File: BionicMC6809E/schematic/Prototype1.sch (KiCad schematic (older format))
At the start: 5 parts, among them J1 BionicConnector, U1 MC6809EP, U2 74HCT126

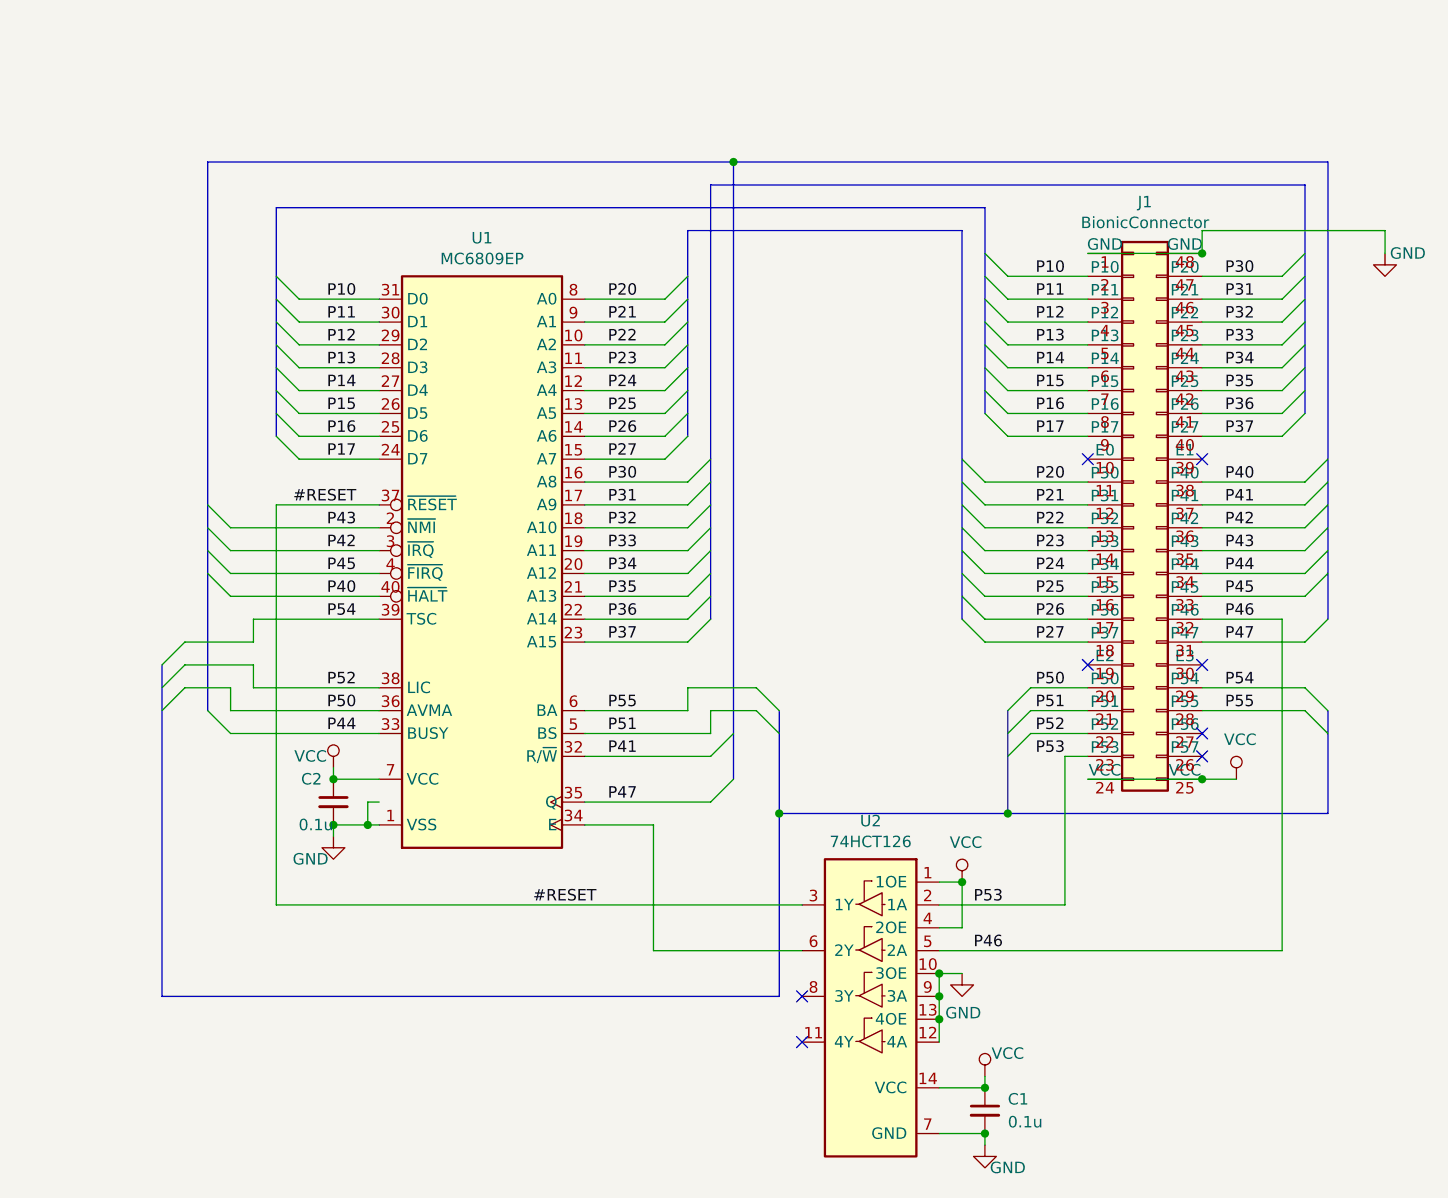
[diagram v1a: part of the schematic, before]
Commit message: [BionicMC6809E] Tune bus cycle
- Teensy 4.1: Q/E ~ 1.0MHz
- Teensy 3.5: Q/E ~ 230kHz
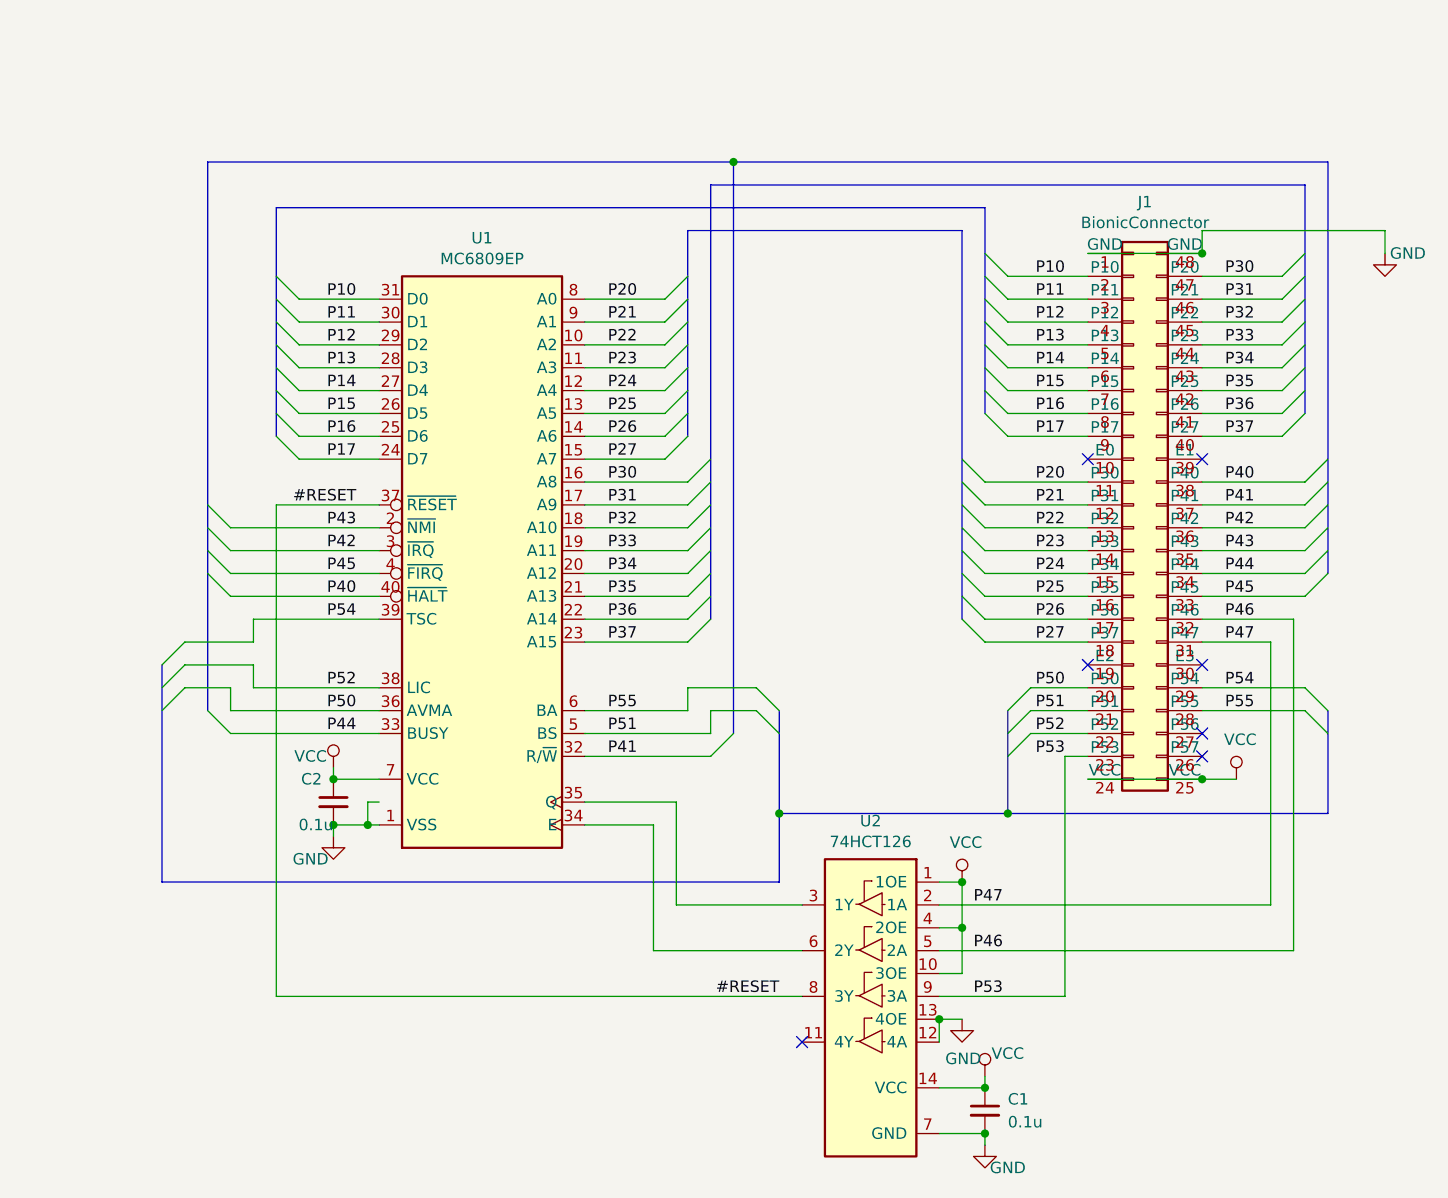
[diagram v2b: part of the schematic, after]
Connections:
- net #RESET: now also U2.8 (3Y); no longer U2.3 (1Y)
- net GND: no longer U2.10 (3OE), U2.9 (3A)
- net P47: now also U2.2 (1A); no longer U1.35 (Q)
- net P53: now also U2.9 (3A); no longer U2.2 (1A)
- net VCC: now also U2.10 (3OE)
- new net: U1.35 (Q), U2.3 (1Y)
- no-connect marks 8 -> 7
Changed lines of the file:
@@
 Sheet 1 1
 Title "BionicMC6809E Mezzanine"
-Date "2021-11-12"
-Rev "1"
+Date "2021-11-25"
+Rev "2"
 Comp "Tadashi G. Takaoka"
 Comment1 ""
@@
 Wire Wire Line
 	7750 2600 7400 2600
-Text Label 6400 4650 0    50   ~ 0
+Text Label 6400 5050 0    50   ~ 0
 P53
 Text Label 3700 3000 2    50   ~ 0
@@
 	1    0    0    -1
 $EndComp
-NoConn ~ 5650 5050
 NoConn ~ 5650 5250
-Text Label 4750 4650 2    50   ~ 0
+Text Label 5550 5050 2    50   ~ 0
 #RESET
 Text Label 3700 2900 2    50   ~ 0
@@
 Entry Wire Line
 	3050 3000 3150 3100
-Entry Wire Line
-	5350 4100 5250 4200
 Text Label 7500 2800 0    50   ~ 0
 P40
@@
 	7400 3300 7850 3300
 Wire Wire Line
-	7400 3500 7850 3500
+	7400 3500 7700 3500
 Entry Wire Line
 	7950 2700 7850 2800
@@
 Entry Wire Line
 	7950 3200 7850 3300
-Entry Wire Line
-	7950 3400 7850 3500
 $Comp
 L power:GND #PWR06
 U 1 1 61A0F5E3
-P 6350 4950
-F 0 "#PWR06" H 6350 4700 50  0001 C CNN
-F 1 "GND" H 6355 4777 50  0000 C CNN
-F 2 "" H 6350 4950 50  0001 C CNN
-F 3 "" H 6350 4950 50  0001 C CNN
-	1    6350 4950
+P 6350 5150
+F 0 "#PWR06" H 6350 4900 50  0001 C CNN
+F 1 "GND" H 6355 4977 50  0000 C CNN
+F 2 "" H 6350 5150 50  0001 C CNN
+F 3 "" H 6350 5150 50  0001 C CNN
+	1    6350 5150
 	1    0    0    -1
 $EndComp
@@
 Text Label 4800 3800 0    50   ~ 0
 P55
-Text Label 4800 4200 0    50   ~ 0
+Text Label 6400 4650 0    50   ~ 0
 P47
-Wire Wire Line
-	5250 4200 4700 4200
 Text Label 3700 3700 2    50   ~ 0
 P52
@@
 Wire Wire Line
 	6250 5250 6250 5150
-Connection ~ 6250 5050
-Wire Wire Line
-	6250 5050 6250 4950
-Connection ~ 6250 5150
-Wire Wire Line
-	6250 5150 6250 5050
-Wire Wire Line
-	6800 4000 6800 4650
 Wire Wire Line
 	3800 3300 3150 3300
@@
 $EndComp
 Wire Wire Line
-	6250 4950 6350 4950
-Connection ~ 6250 4950
-Wire Wire Line
 	6350 4750 6250 4750
 Connection ~ 6350 4550
@@
 	6350 4550 6350 4750
 Wire Wire Line
-	7400 3400 7750 3400
-Wire Wire Line
-	7750 3400 7750 4850
-Wire Wire Line
-	7750 4850 6250 4850
-Text Label 6400 4850 0    50   ~ 0
-P46
+	7400 3400 7800 3400
+Wire Wire Line
+	7800 3400 7800 4850
+Wire Wire Line
+	7800 4850 6250 4850
 Wire Wire Line
 	4700 4300 5000 4300
@@
 Wire Bus Line
 	3350 1600 6450 1600
-Wire Bus Line
-	3050 1400 5350 1400
-Connection ~ 5350 1400
-Wire Bus Line
-	5350 1400 7950 1400
 Entry Wire Line
 	3150 3900 3050 3800
@@
 	3800 3900 3150 3900
 Wire Wire Line
-	3350 2900 3350 4650
-Wire Wire Line
 	3350 2900 3800 2900
 Wire Wire Line
-	3350 4650 5650 4650
+	3350 5050 5650 5050
 Text Label 3700 3800 2    50   ~ 0
 P50
@@
 Wire Wire Line
 	6800 4000 6900 4000
-Wire Wire Line
-	6250 4650 6800 4650
 Entry Wire Line
 	6550 3800 6650 3700
@@
 	6550 4250 5550 4250
 Wire Bus Line
-	5550 4250 5550 5050
-Wire Bus Line
-	5550 5050 2850 5050
-Wire Bus Line
-	5350 1400 5350 4100
+	5550 4250 5550 4550
+Wire Bus Line
+	5550 4550 2850 4550
+Connection ~ 5550 4250
+Wire Wire Line
+	6250 5150 6350 5150
+Connection ~ 6250 5150
+Text Label 6400 4850 0    50   ~ 0
+P46
+Wire Wire Line
+	6350 4750 6350 4950
+Wire Wire Line
+	6350 4950 6250 4950
+Connection ~ 6350 4750
+Wire Wire Line
+	6800 5050 6250 5050
+Wire Wire Line
+	6800 4000 6800 5050
+Wire Wire Line
+	7700 3500 7700 4650
+Wire Wire Line
+	7700 4650 6250 4650
+Wire Wire Line
+	3350 2900 3350 5050
+Wire Bus Line
+	3050 1400 5350 1400
+Wire Wire Line
+	5100 4200 5100 4650
+Wire Wire Line
+	5100 4650 5650 4650
+Wire Wire Line
+	5100 4200 4700 4200
+Wire Bus Line
+	5350 3900 5350 1400
 Wire Bus Line
 	7950 3800 7950 4250
@@
 	5550 3800 5550 4250
 Wire Bus Line
-	2850 3600 2850 5050
+	2850 3600 2850 4550
 Wire Bus Line
 	6550 3800 6550 4250
@@
 	3050 1400 3050 3800
 Wire Bus Line
-	7950 1400 7950 3400
+	7950 1400 7950 3200
 Wire Bus Line
 	5250 1500 5250 3400
@@
 Wire Bus Line
 	3350 1600 3350 2600
-Connection ~ 5550 4250
+Connection ~ 5350 1400
+Wire Bus Line
+	5350 1400 7950 1400
 $EndSCHEMATC

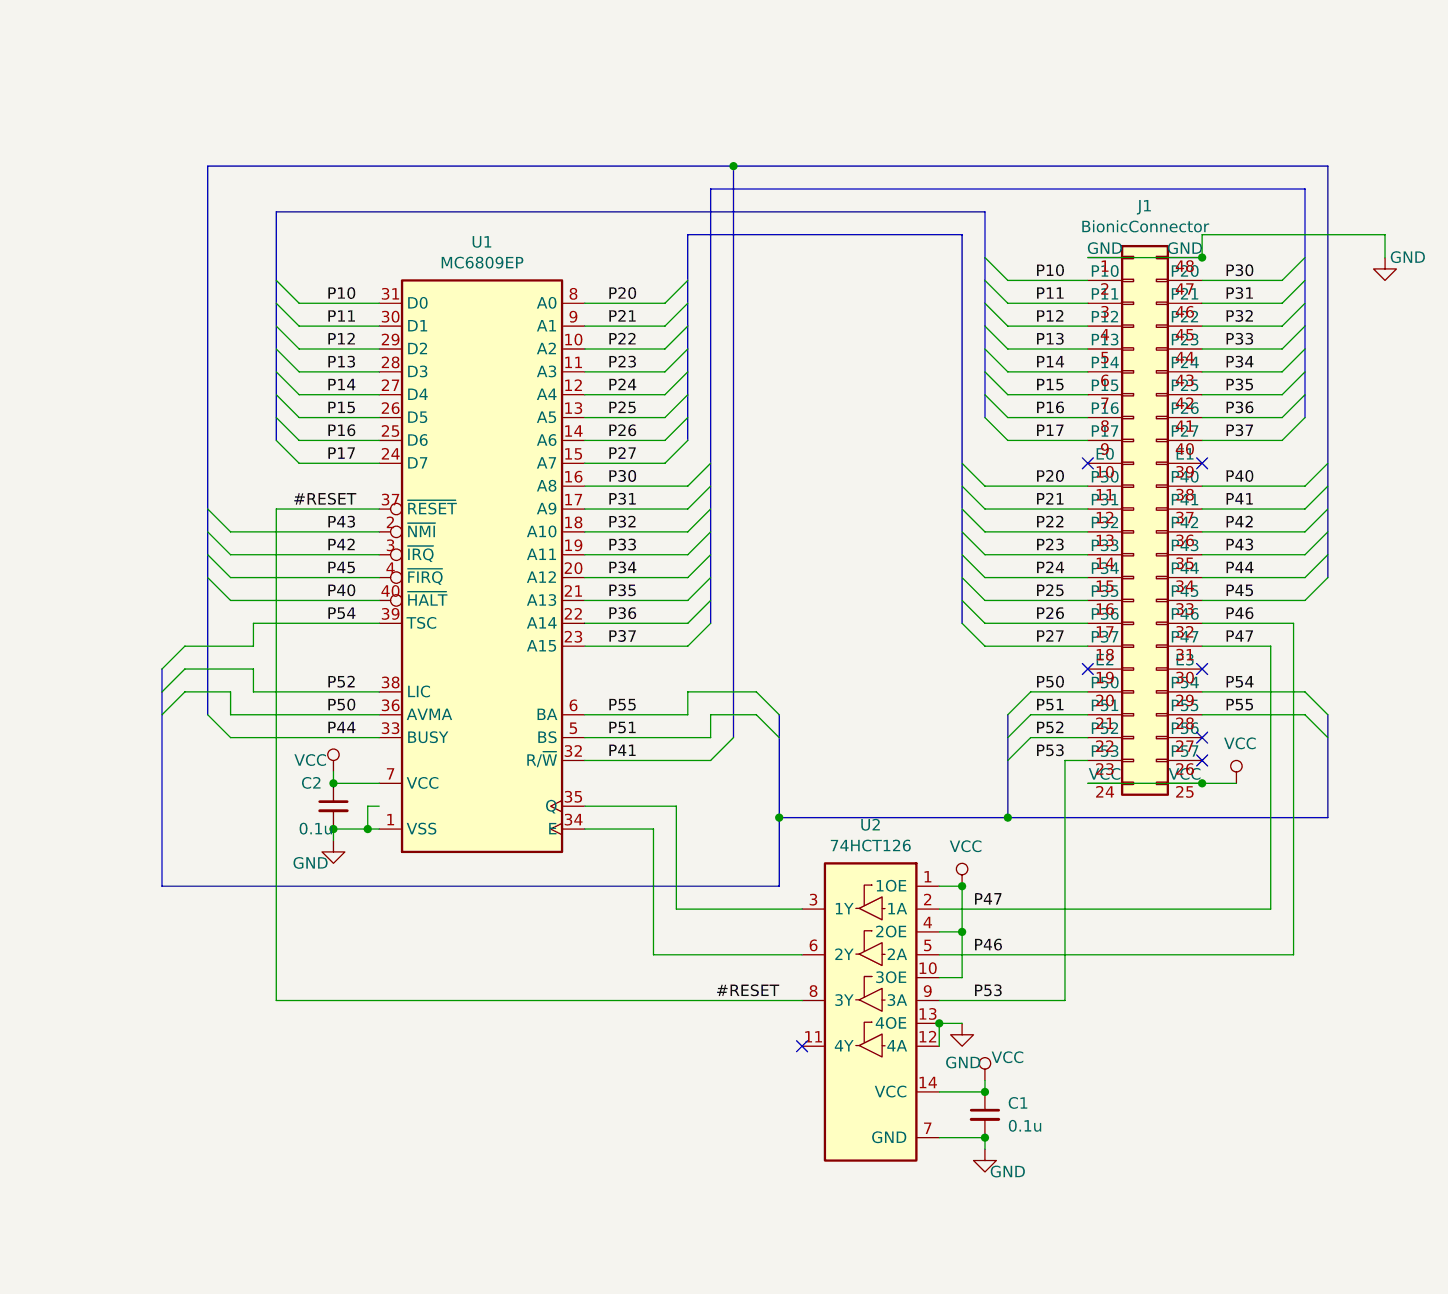
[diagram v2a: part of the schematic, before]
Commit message: Fix Bionic connector pin outs
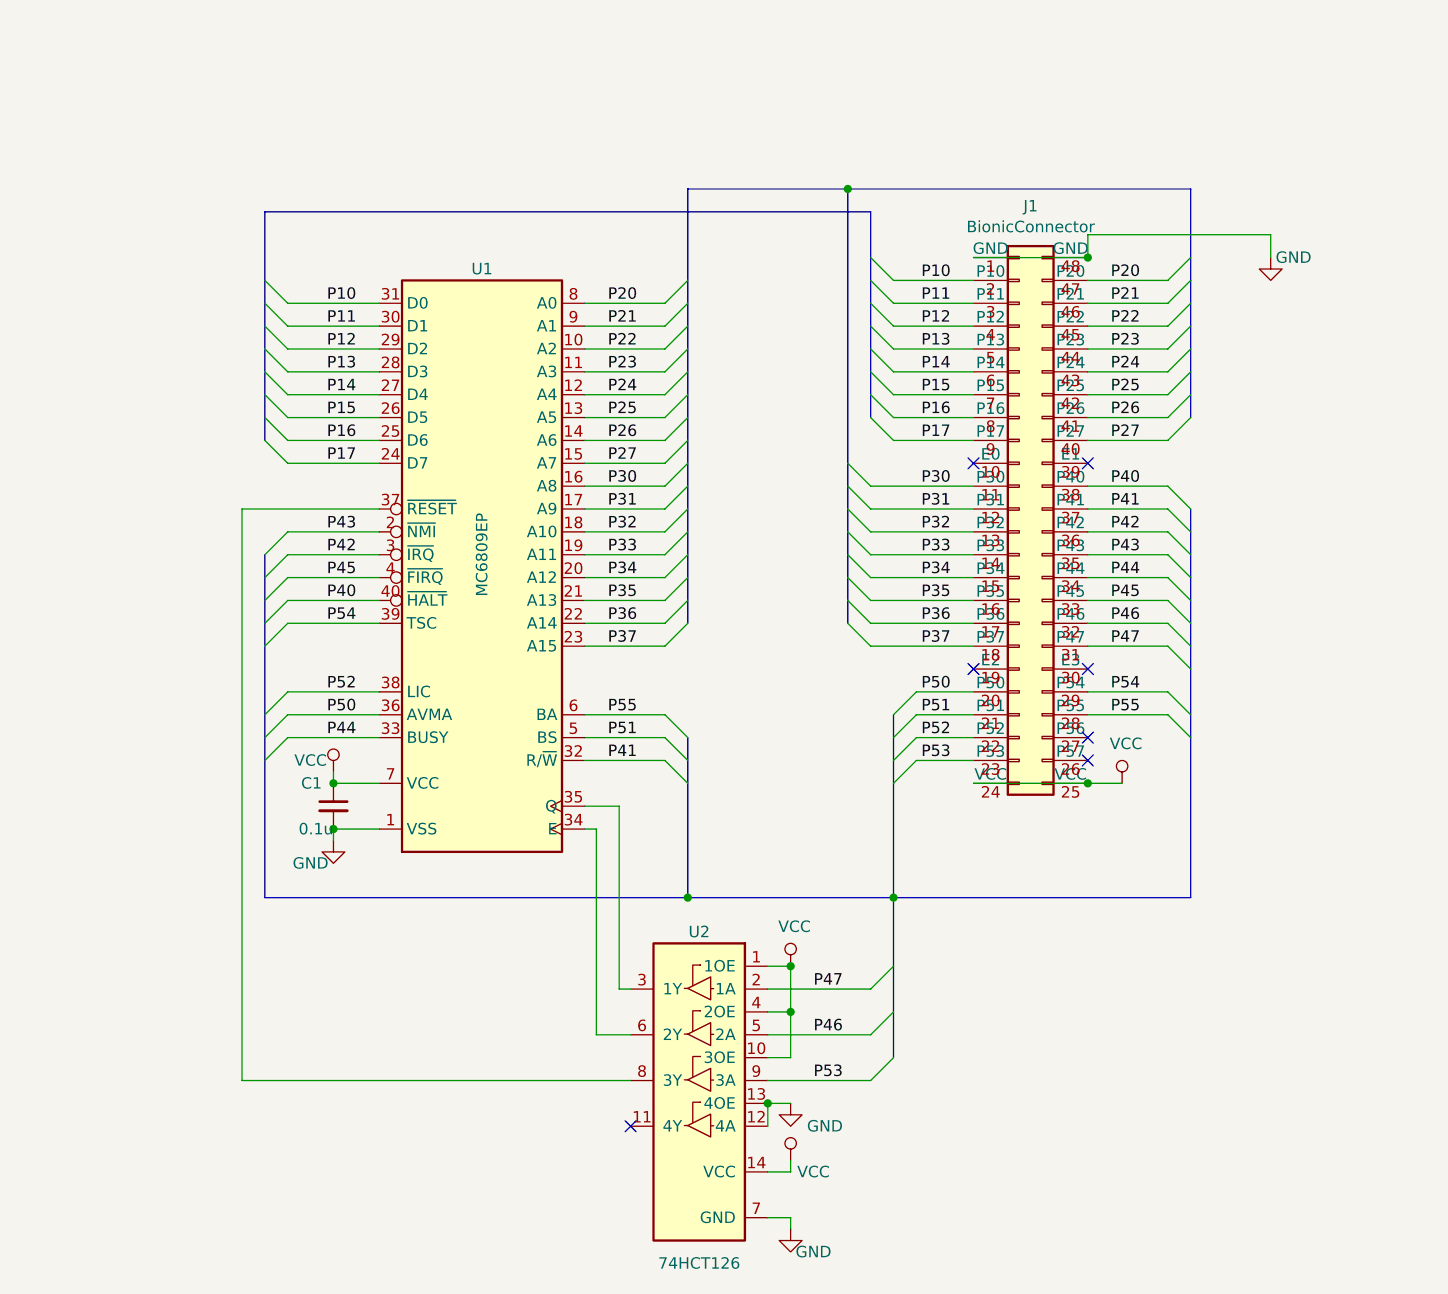
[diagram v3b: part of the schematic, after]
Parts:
- removed C1: 0.1u, Capacitor_THT:C_Disc_D3.4mm_W2.1mm_P2.50mm, symbol Device:C_Small
- renumbered C2 to C1
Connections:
- net P20: now also J1.47 (P20); no longer J1.11 (P30)
- net P21: now also J1.46 (P21); no longer J1.12 (P31)
- net P22: now also J1.45 (P22); no longer J1.13 (P32)
- net P23: now also J1.44 (P23); no longer J1.14 (P33)
- net P24: now also J1.43 (P24); no longer J1.15 (P34)
- net P25: now also J1.42 (P25); no longer J1.16 (P35)
- net P26: now also J1.41 (P26); no longer J1.17 (P36)
- net P27: now also J1.40 (P27); no longer J1.18 (P37)
- net P30: now also J1.11 (P30); no longer J1.47 (P20)
- net P31: now also J1.12 (P31); no longer J1.46 (P21)
- net P32: now also J1.13 (P32); no longer J1.45 (P22)
- net P33: now also J1.14 (P33); no longer J1.44 (P23)
- net P34: now also J1.15 (P34); no longer J1.43 (P24)
- net P35: now also J1.16 (P35); no longer J1.42 (P25)
- net P36: now also J1.17 (P36); no longer J1.41 (P26)
- net P37: now also J1.18 (P37); no longer J1.40 (P27)
- net #RESET: no longer names the net of U1.37 (~RESET), U2.8 (3Y)
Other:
- moved on the sheet: U2
